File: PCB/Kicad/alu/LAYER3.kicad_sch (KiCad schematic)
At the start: 4 parts, among them U37 74LS257, U38 74LS257, U39 74LS257, U40 74LS257

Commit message: UPDATE
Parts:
- added C34, C35, C36, C37: 10n, symbol Device:C
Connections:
- net L010 is gone; now on net Lin13: U39.6 (I1b)
- net GND: now also U40.13 (I1c), U40.3 (I1a), U40.6 (I1b), C34.2, C35.2, C36.2, C37.2
- net Lin1: no longer U37.3 (I1a)
- net Lin10: now also U38.13 (I1c)
- net Lin11: now also U38.10 (I1d); no longer U39.13 (I1c)
- net Lin12: now also U39.3 (I1a); no longer U39.10 (I1d)
- net Lin13: no longer U40.3 (I1a)
- net Lin14: now also U39.13 (I1c); no longer U40.6 (I1b)
- net Lin15: now also U39.10 (I1d); no longer U40.13 (I1c)
- net Lin2: no longer U37.6 (I1b)
- net Lin3: no longer U37.13 (I1c)
- net Lin4: now also U37.3 (I1a); no longer U37.10 (I1d)
- net Lin5: now also U37.6 (I1b); no longer U38.3 (I1a)
- net Lin6: now also U37.13 (I1c); no longer U38.6 (I1b)
- net Lin7: now also U37.10 (I1d); no longer U38.13 (I1c)
- net Lin8: now also U38.3 (I1a); no longer U38.10 (I1d)
- net Lin9: now also U38.6 (I1b); no longer U39.3 (I1a)
- net VCC: now also C34.1, C35.1, C36.1, C37.1

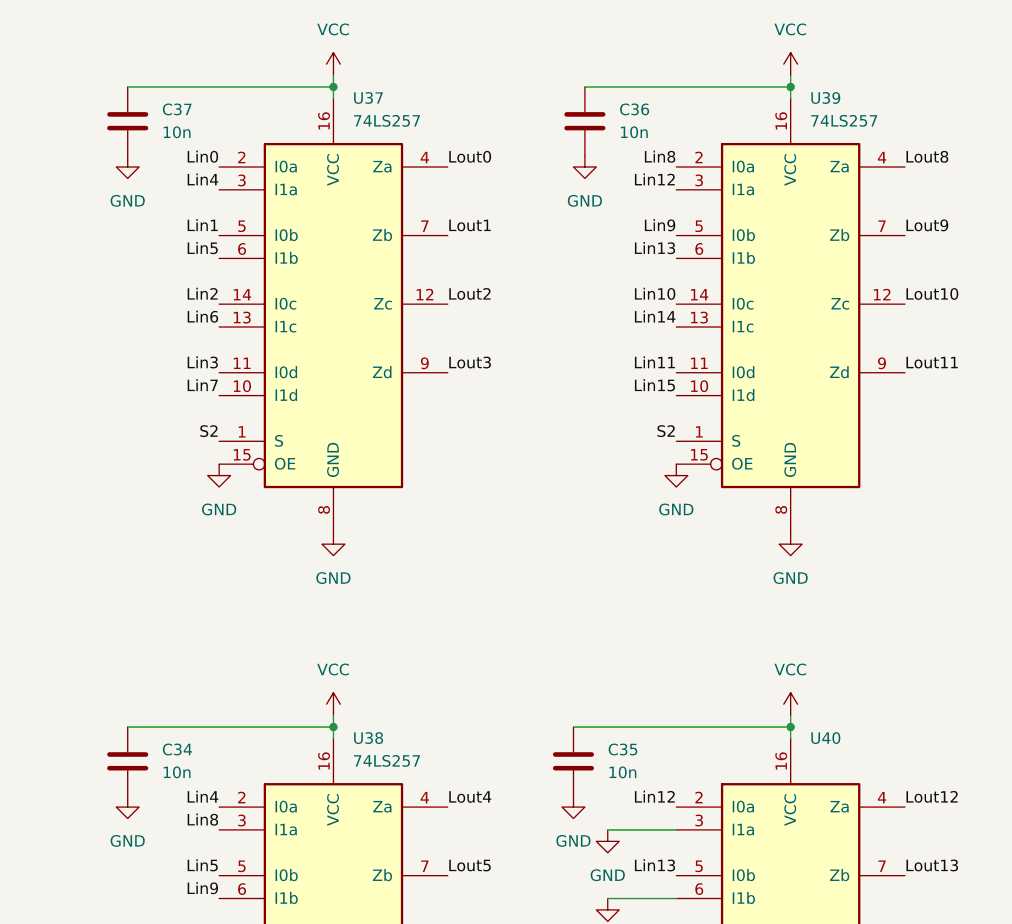
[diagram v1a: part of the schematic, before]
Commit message: LEDs added
REGISTER.kicad_sch LEDs added to both REG_A and REG_B
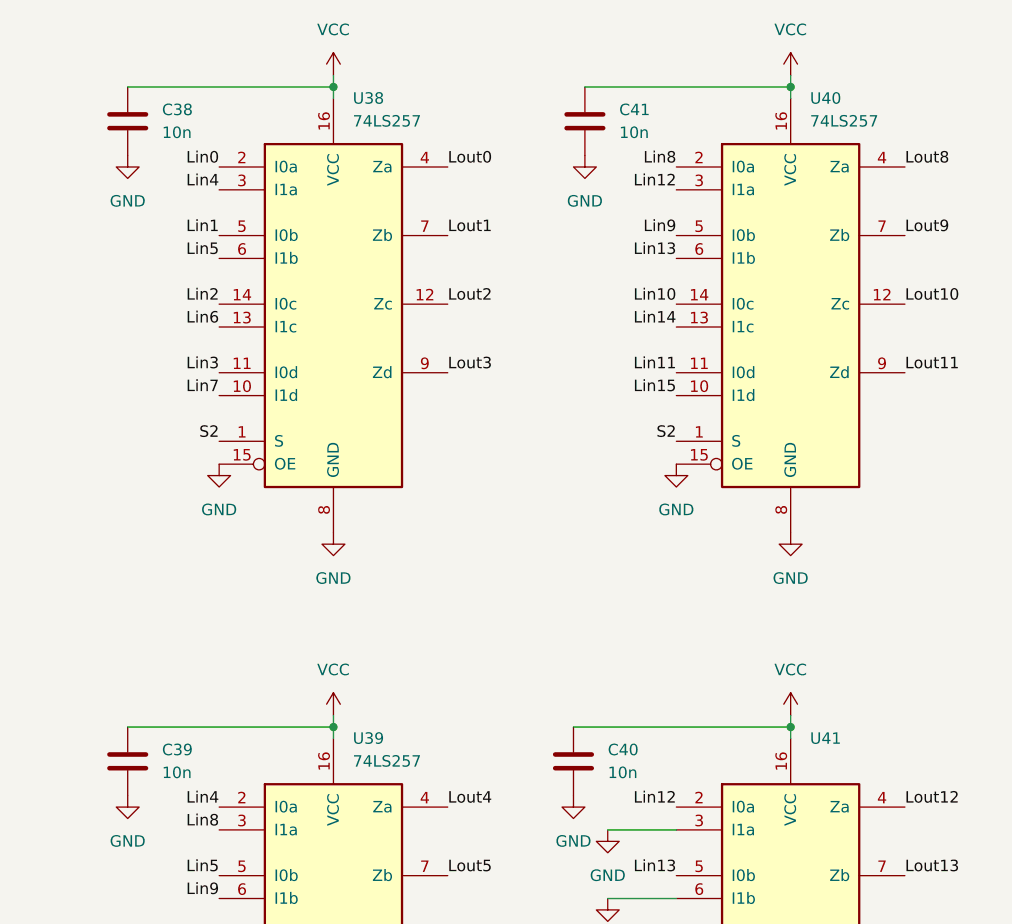
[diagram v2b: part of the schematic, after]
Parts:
- renumbered C37 to C38, C34 to C39, C35 to C40, C36 to C41, U37 to U38, U38 to U39, U39 to U40, U40 to U41

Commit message: Footprints, PCB update
Added footprints to all components, updated the PCB with the schematic
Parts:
- C38, C39, C40, C41: footprint (none) -> Capacitor_SMD:C_0603_1608Metric
- U38, U39, U40, U41: footprint (none) -> Package_SO:SOIC-16_3.9x9.9mm_P1.27mm
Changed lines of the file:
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@@
 			)
 		)
-		(property "Footprint" ""
+		(property "Footprint" "Package_SO:SOIC-16_3.9x9.9mm_P1.27mm"
 			(at 109.22 54.61 0)
 			(effects
@@
 			)
 		)
-		(property "Footprint" ""
+		(property "Footprint" "Capacitor_SMD:C_0603_1608Metric"
 			(at 87.3252 38.1 0)
 			(effects
@@
 			)
 		)
-		(property "Footprint" ""
+		(property "Footprint" "Package_SO:SOIC-16_3.9x9.9mm_P1.27mm"
 			(at 160.02 54.61 0)
 			(effects
@@
 			)
 		)
-		(property "Footprint" ""
+		(property "Footprint" "Package_SO:SOIC-16_3.9x9.9mm_P1.27mm"
 			(at 109.22 125.73 0)
 			(effects
@@
 			)
 		)
-		(property "Footprint" ""
+		(property "Footprint" "Package_SO:SOIC-16_3.9x9.9mm_P1.27mm"
 			(at 160.02 125.73 0)
 			(effects
@@
 			)
 		)
-		(property "Footprint" ""
+		(property "Footprint" "Capacitor_SMD:C_0603_1608Metric"
 			(at 138.1252 38.1 0)
 			(effects
@@
 			)
 		)
-		(property "Footprint" ""
+		(property "Footprint" "Capacitor_SMD:C_0603_1608Metric"
 			(at 136.8552 109.22 0)
 			(effects
@@
 			)
 		)
-		(property "Footprint" ""
+		(property "Footprint" "Capacitor_SMD:C_0603_1608Metric"
 			(at 87.3252 109.22 0)
 			(effects

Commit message: ALU Pcb update
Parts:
- C38, C39, C40, C41: value 10n -> 100nF; footprint Capacitor_SMD:C_0603_1608Metric -> Capacitor_SMD:C_0402_1005Metric
- U38, U39, U40, U41: value 74LS257 -> 74257
